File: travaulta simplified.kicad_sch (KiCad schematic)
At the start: 26 parts, among them SW38 BOOT0, U1 STM32F411CCUx, U2 XC6206PxxxMR, Y1 16 MHz

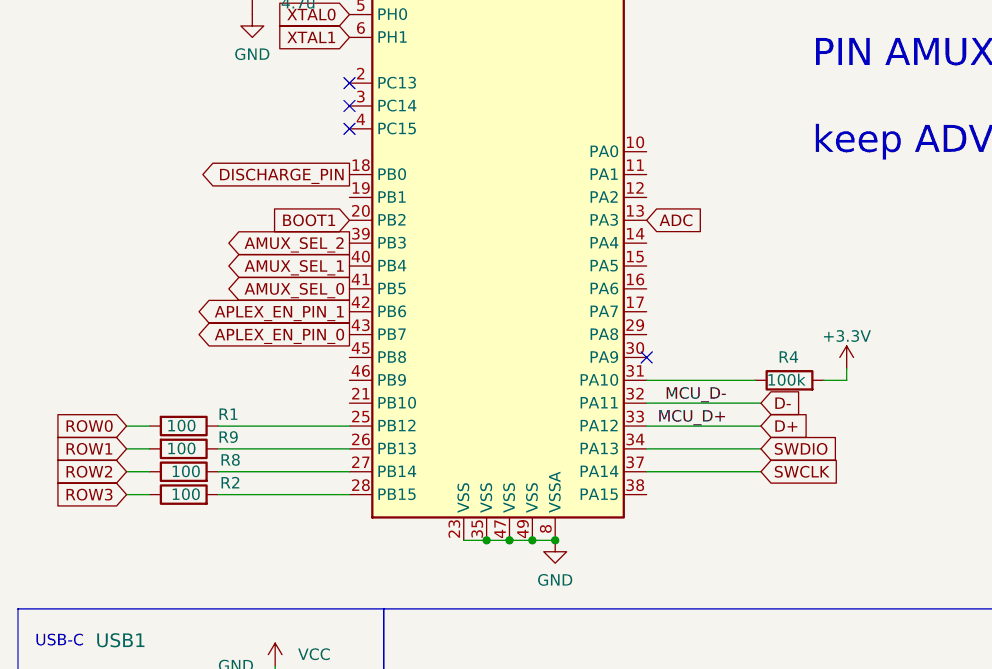
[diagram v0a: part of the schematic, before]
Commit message: cleaned pcb, silkscreen, created first plates
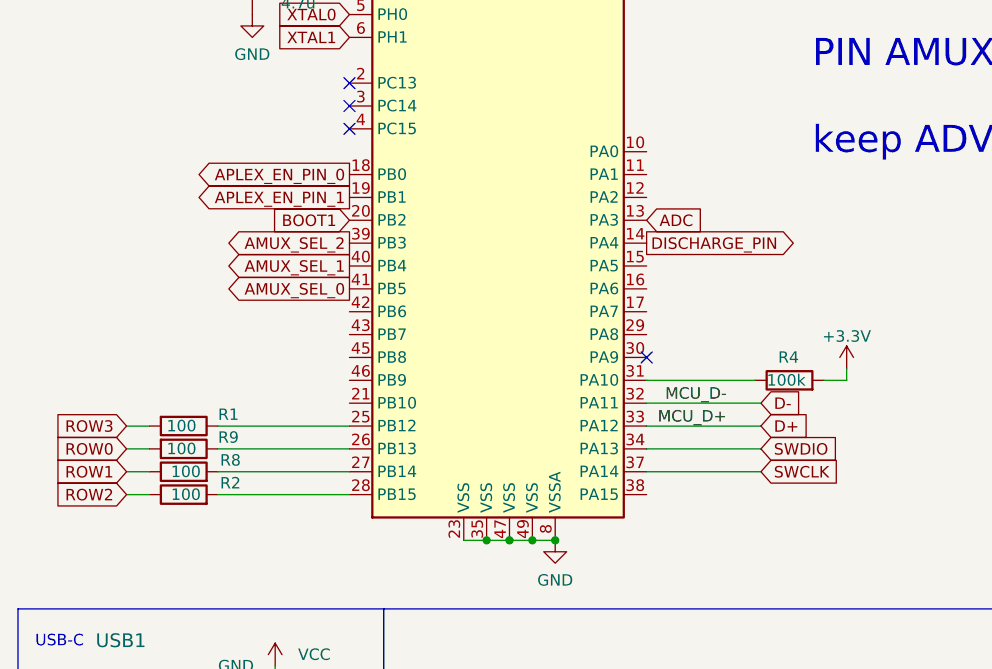
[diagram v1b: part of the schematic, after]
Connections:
- net APLEX_EN_PIN_0: now also U1.18 (PB0); no longer U1.43 (PB7)
- net APLEX_EN_PIN_1: now also U1.19 (PB1); no longer U1.42 (PB6)
- net DISCHARGE_PIN: now also U1.14 (PA4); no longer U1.18 (PB0)
- net ROW0: now also R9.2; no longer R1.2
- net ROW1: now also R8.1; no longer R9.2
- net ROW2: now also R2.1; no longer R8.1
- net ROW3: now also R1.2; no longer R2.1
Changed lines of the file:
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@@
     )
   )
-  (global_label "ROW0" (shape input) (at 24.13 86.995 180) (fields_autoplaced)
+  (global_label "ROW0" (shape input) (at 24.13 89.535 180) (fields_autoplaced)
     (effects (font (size 1.27 1.27)) (justify right))
-    (property "Intersheetrefs" "${INTERSHEET_REFS}" (at 16.4555 86.9156 0)
+    (property "Intersheetrefs" "${INTERSHEET_REFS}" (at 16.4555 89.4556 0)
       (effects (font (size 1.27 1.27)) (justify right) hide)
     )
   )
-  (global_label "DISCHARGE_PIN" (shape output) (at 48.895 59.055 180) (fields_autoplaced)
-    (effects (font (size 1.27 1.27)) (justify right))
-    (property "Intersheetrefs" "${INTERSHEET_REFS}" (at 31.8467 58.9756 0)
-      (effects (font (size 1.27 1.27)) (justify right) hide)
+  (global_label "DISCHARGE_PIN" (shape output) (at 81.915 66.675 0) (fields_autoplaced)
+    (effects (font (size 1.27 1.27)) (justify left))
+    (property "Intersheetrefs" "${INTERSHEET_REFS}" (at 99.4561 66.675 0)
+      (effects (font (size 1.27 1.27)) (justify left) hide)
     )
   )
@@
     )
   )
-  (global_label "ROW2" (shape input) (at 24.13 92.075 180) (fields_autoplaced)
+  (global_label "ROW2" (shape input) (at 24.13 94.615 180) (fields_autoplaced)
     (effects (font (size 1.27 1.27)) (justify right))
-    (property "Intersheetrefs" "${INTERSHEET_REFS}" (at 16.4555 92.1544 0)
+    (property "Intersheetrefs" "${INTERSHEET_REFS}" (at 16.4555 94.6944 0)
       (effects (font (size 1.27 1.27)) (justify right) hide)
     )
@@
     )
   )
-  (global_label "ROW1" (shape input) (at 24.13 89.535 180) (fields_autoplaced)
+  (global_label "ROW1" (shape input) (at 24.13 92.075 180) (fields_autoplaced)
     (effects (font (size 1.27 1.27)) (justify right))
-    (property "Intersheetrefs" "${INTERSHEET_REFS}" (at 16.4555 89.6144 0)
+    (property "Intersheetrefs" "${INTERSHEET_REFS}" (at 16.4555 92.1544 0)
       (effects (font (size 1.27 1.27)) (justify right) hide)
     )
@@
     )
   )
-  (global_label "APLEX_EN_PIN_0" (shape output) (at 48.895 76.835 180) (fields_autoplaced)
+  (global_label "APLEX_EN_PIN_0" (shape output) (at 48.895 59.055 180) (fields_autoplaced)
     (effects (font (size 1.27 1.27)) (justify right))
-    (property "Intersheetrefs" "${INTERSHEET_REFS}" (at 30.9395 76.7556 0)
+    (property "Intersheetrefs" "${INTERSHEET_REFS}" (at 30.4469 59.055 0)
       (effects (font (size 1.27 1.27)) (justify right) hide)
     )
@@
     )
   )
-  (global_label "APLEX_EN_PIN_1" (shape output) (at 48.895 74.295 180) (fields_autoplaced)
+  (global_label "APLEX_EN_PIN_1" (shape output) (at 48.895 61.595 180) (fields_autoplaced)
     (effects (font (size 1.27 1.27)) (justify right))
-    (property "Intersheetrefs" "${INTERSHEET_REFS}" (at 30.9395 74.2156 0)
+    (property "Intersheetrefs" "${INTERSHEET_REFS}" (at 30.9395 61.5156 0)
       (effects (font (size 1.27 1.27)) (justify right) hide)
     )
   )
-  (global_label "ROW3" (shape input) (at 24.13 94.615 180) (fields_autoplaced)
+  (global_label "ROW3" (shape input) (at 24.13 86.995 180) (fields_autoplaced)
     (effects (font (size 1.27 1.27)) (justify right))
-    (property "Intersheetrefs" "${INTERSHEET_REFS}" (at 16.4555 94.5356 0)
+    (property "Intersheetrefs" "${INTERSHEET_REFS}" (at 16.4555 86.9156 0)
       (effects (font (size 1.27 1.27)) (justify right) hide)
     )

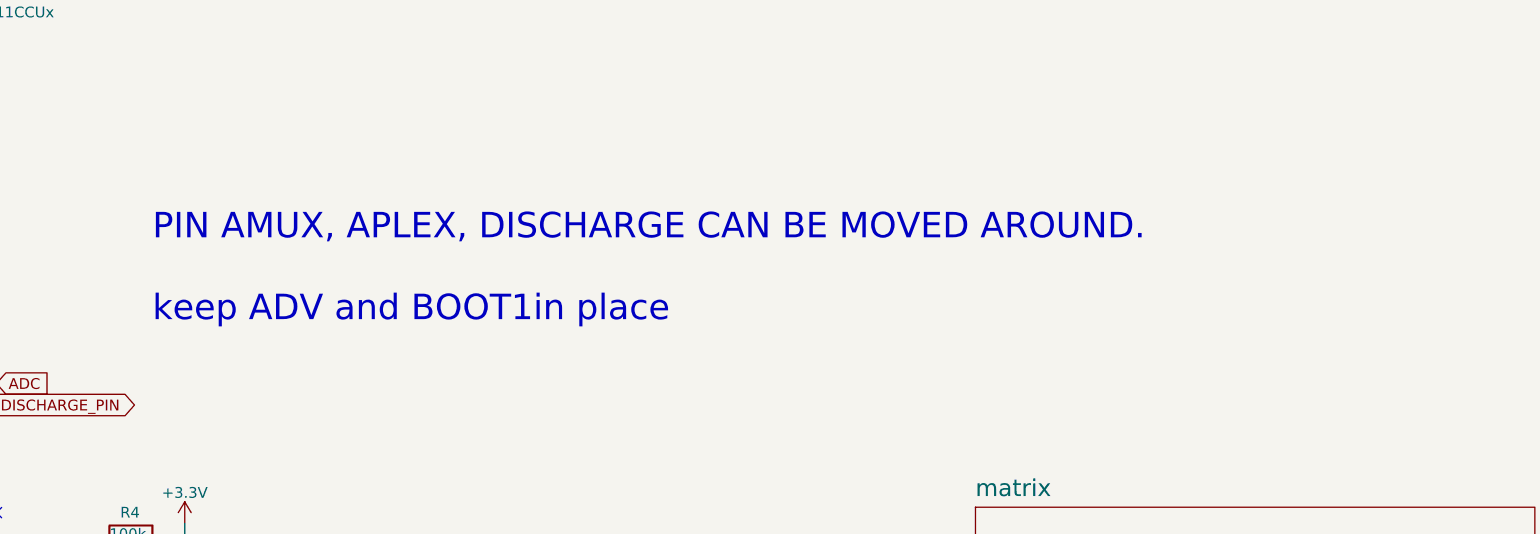
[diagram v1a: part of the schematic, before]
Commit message: created more plates
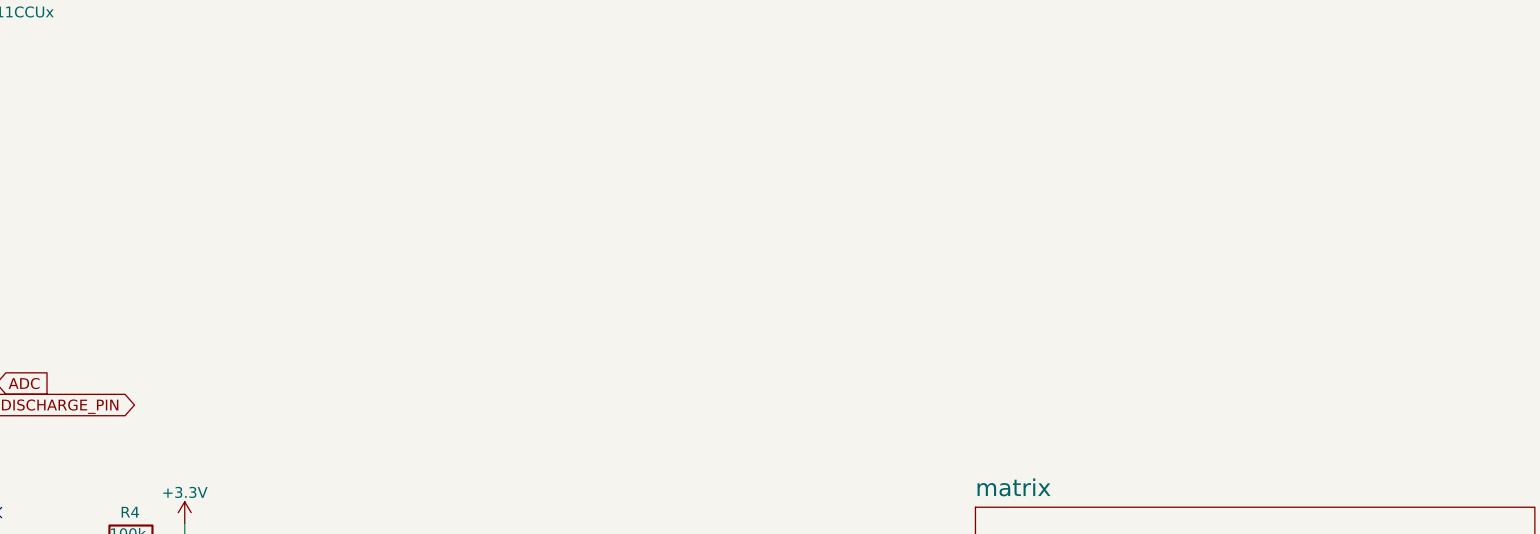
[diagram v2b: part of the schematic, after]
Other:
- note removed: "PIN AMUX, APLEX, DISCHARGE CAN BE MOVED AROUND. keep ADV and BOOT1in place"
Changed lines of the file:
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@@
     (effects (font (size 2 2)) (justify left bottom))
-  )
-  (text "PIN AMUX, APLEX, DISCHARGE CAN BE MOVED AROUND.\n\nkeep ADV and BOOT1in place"
-    (at 100.33 57.15 0)
-    (effects (font (size 3 3)) (justify left bottom))
   )
   (text "Crystal" (at 94.615 167.64 0)
